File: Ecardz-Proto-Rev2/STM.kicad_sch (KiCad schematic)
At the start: 28 parts, among them J1 Conn_02x06_Odd_Even, J3 Conn_01x06, U1 STM32L071K8Ux

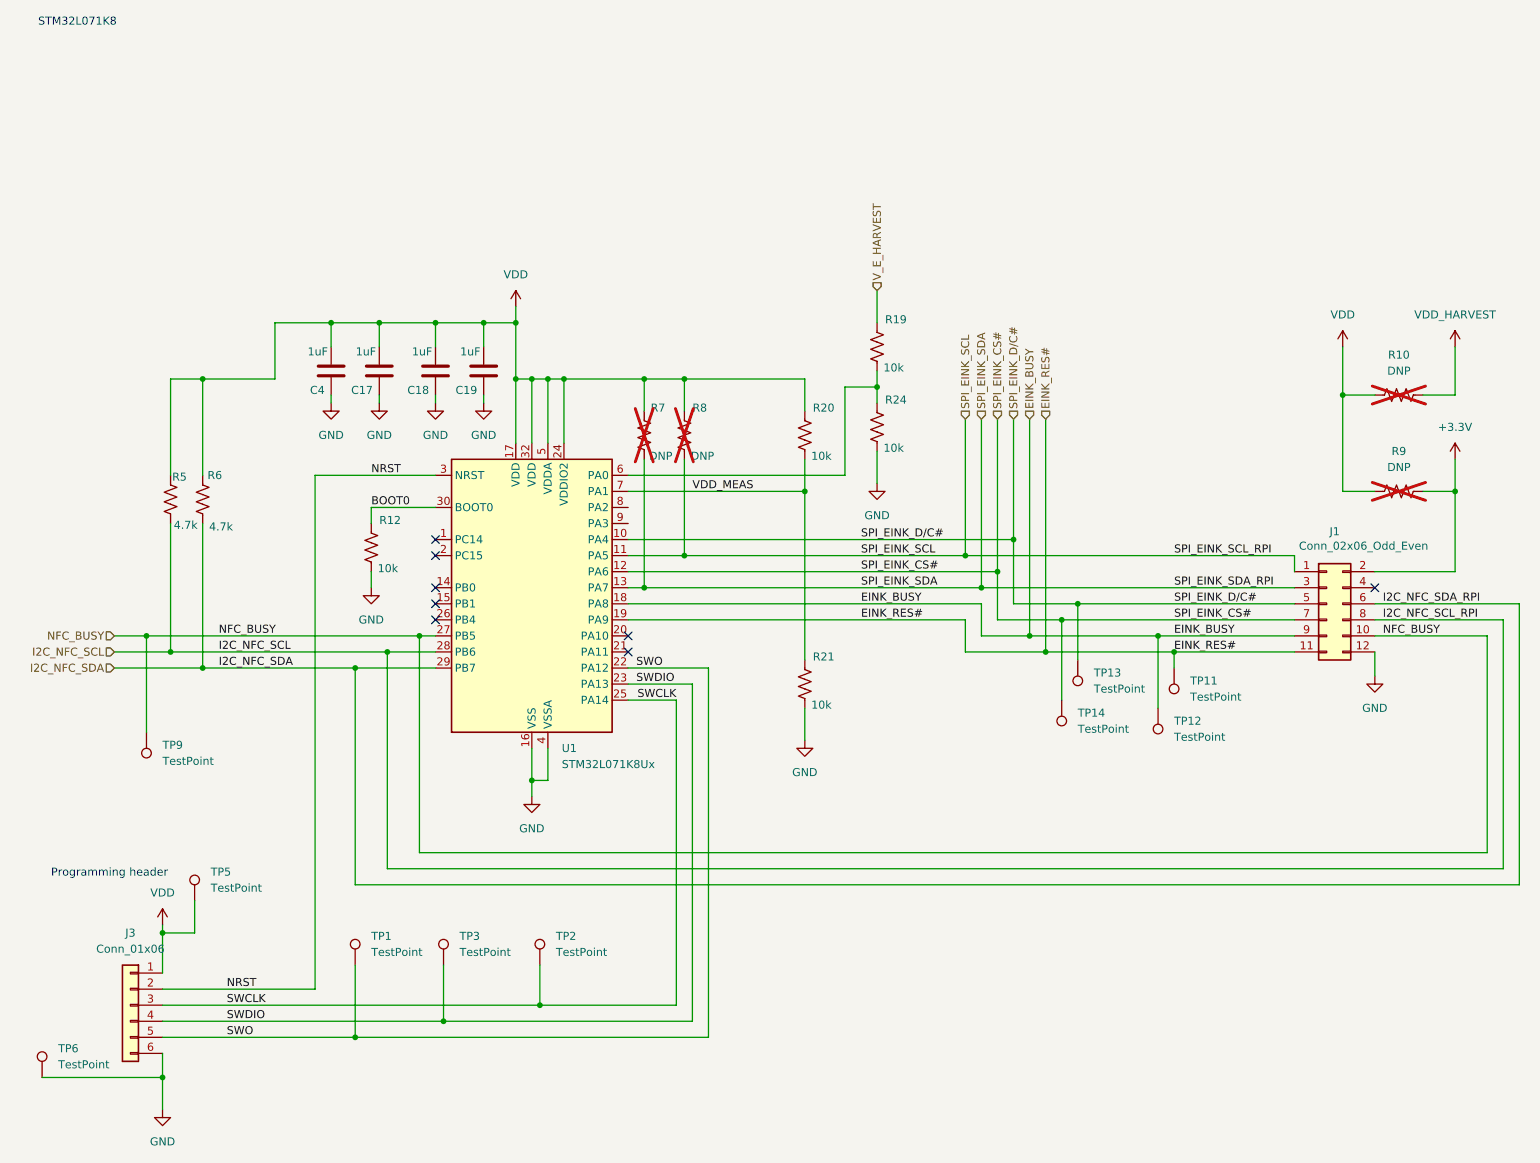
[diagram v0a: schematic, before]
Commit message: most of layout complete
switched ADC pins for ease of layout. added LEDs
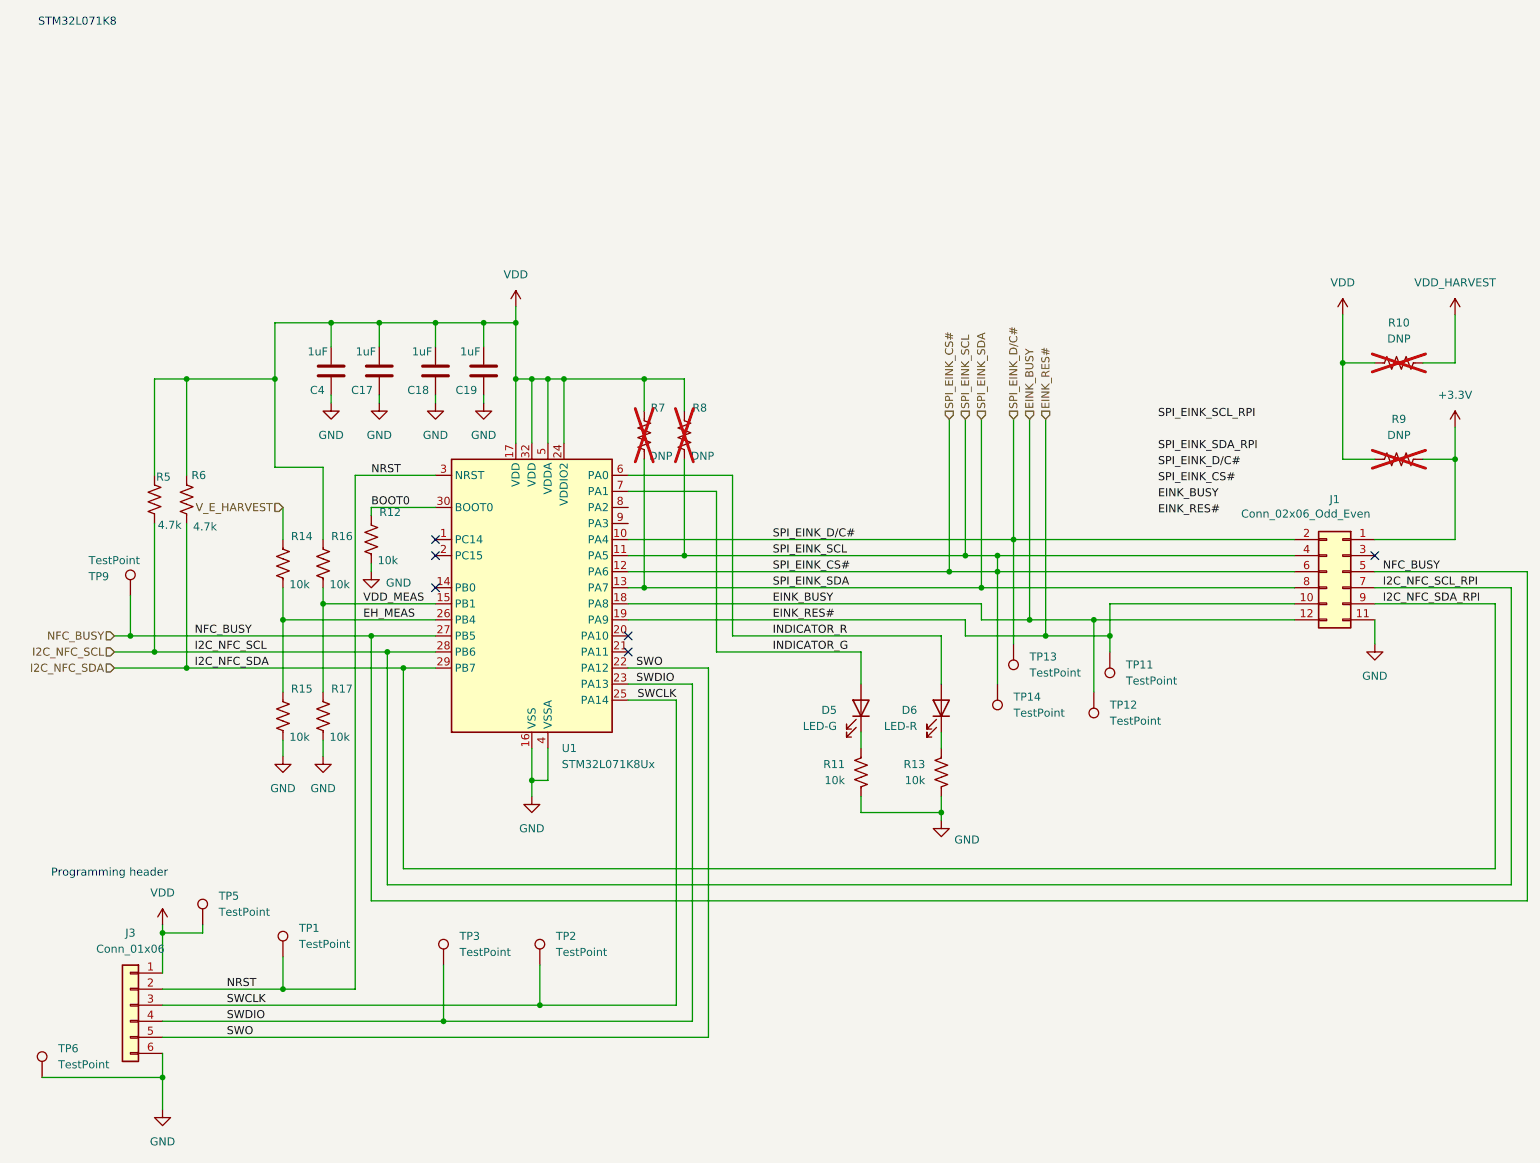
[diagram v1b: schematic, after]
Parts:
- removed R19, R20, R21, R24: 10k, Resistor_SMD:R_0603_1608Metric_Pad0.98x0.95mm_HandSolder, symbol Device:R_US
- added D5: LED-G, LED_SMD:LED_0603_1608Metric_Pad1.05x0.95mm_HandSolder, symbol Device:LED
- added D6: LED-R, LED_SMD:LED_0603_1608Metric_Pad1.05x0.95mm_HandSolder, symbol Device:LED
- added R11, R13, R14, R15, R16, R17: 10k, Resistor_SMD:R_0603_1608Metric_Pad0.98x0.95mm_HandSolder, symbol Device:R_US
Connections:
- net +3.3V: now also J1.1 (Pin_1); no longer J1.2 (Pin_2)
- net EINK_BUSY: now also J1.12 (Pin_12); no longer J1.9 (Pin_9)
- net EINK_RES#: now also J1.10 (Pin_10); no longer J1.11 (Pin_11)
- net GND: now also J1.11 (Pin_11), R11.2, R13.2, R15.2, R17.2; no longer J1.12 (Pin_12)
- net I2C_NFC_SCL: now also J1.7 (Pin_7); no longer J1.8 (Pin_8)
- net I2C_NFC_SDA: now also J1.9 (Pin_9); no longer J1.6 (Pin_6)
- net NFC_BUSY: now also J1.5 (Pin_5); no longer J1.10 (Pin_10)
- net NRST: now also TP1.1
- net SPI_EINK_CS#: now also J1.4 (Pin_4), J1.6 (Pin_6), R8.2, U1.11 (PA5); no longer J1.7 (Pin_7)
- net SPI_EINK_D/C#: now also J1.2 (Pin_2); no longer J1.5 (Pin_5)
- net SPI_EINK_SDA: now also J1.8 (Pin_8); no longer J1.3 (Pin_3)
- net SWO: no longer TP1.1
- net VDD: now also R16.1
- net VDD_MEAS: now also U1.15 (PB1), R16.2, R17.1; no longer U1.7 (PA1)
- net V_E_HARVEST: now also R14.1
- net INDICATOR_R: now reaches U1.6 (PA0)
- net INDICATOR_R: now also D6.2 (A)
- net EH_MEAS: now reaches U1.26 (PB4)
- net EH_MEAS: now also R14.2, R15.1
- removed net SPI_EINK_SCL: J1.1 (Pin_1), R8.2, U1.11 (PA5)
- new net: D6.1 (K), R13.1
- new net: D5.1 (K), R11.1
- new net INDICATOR_G: D5.2 (A), U1.7 (PA1)
- no-connect marks 8 -> 6
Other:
- moved on the sheet: R10, R12, R5, R6, R9, TP1, TP11, TP12, TP13, TP14, TP5, TP9

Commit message: removed RPI header
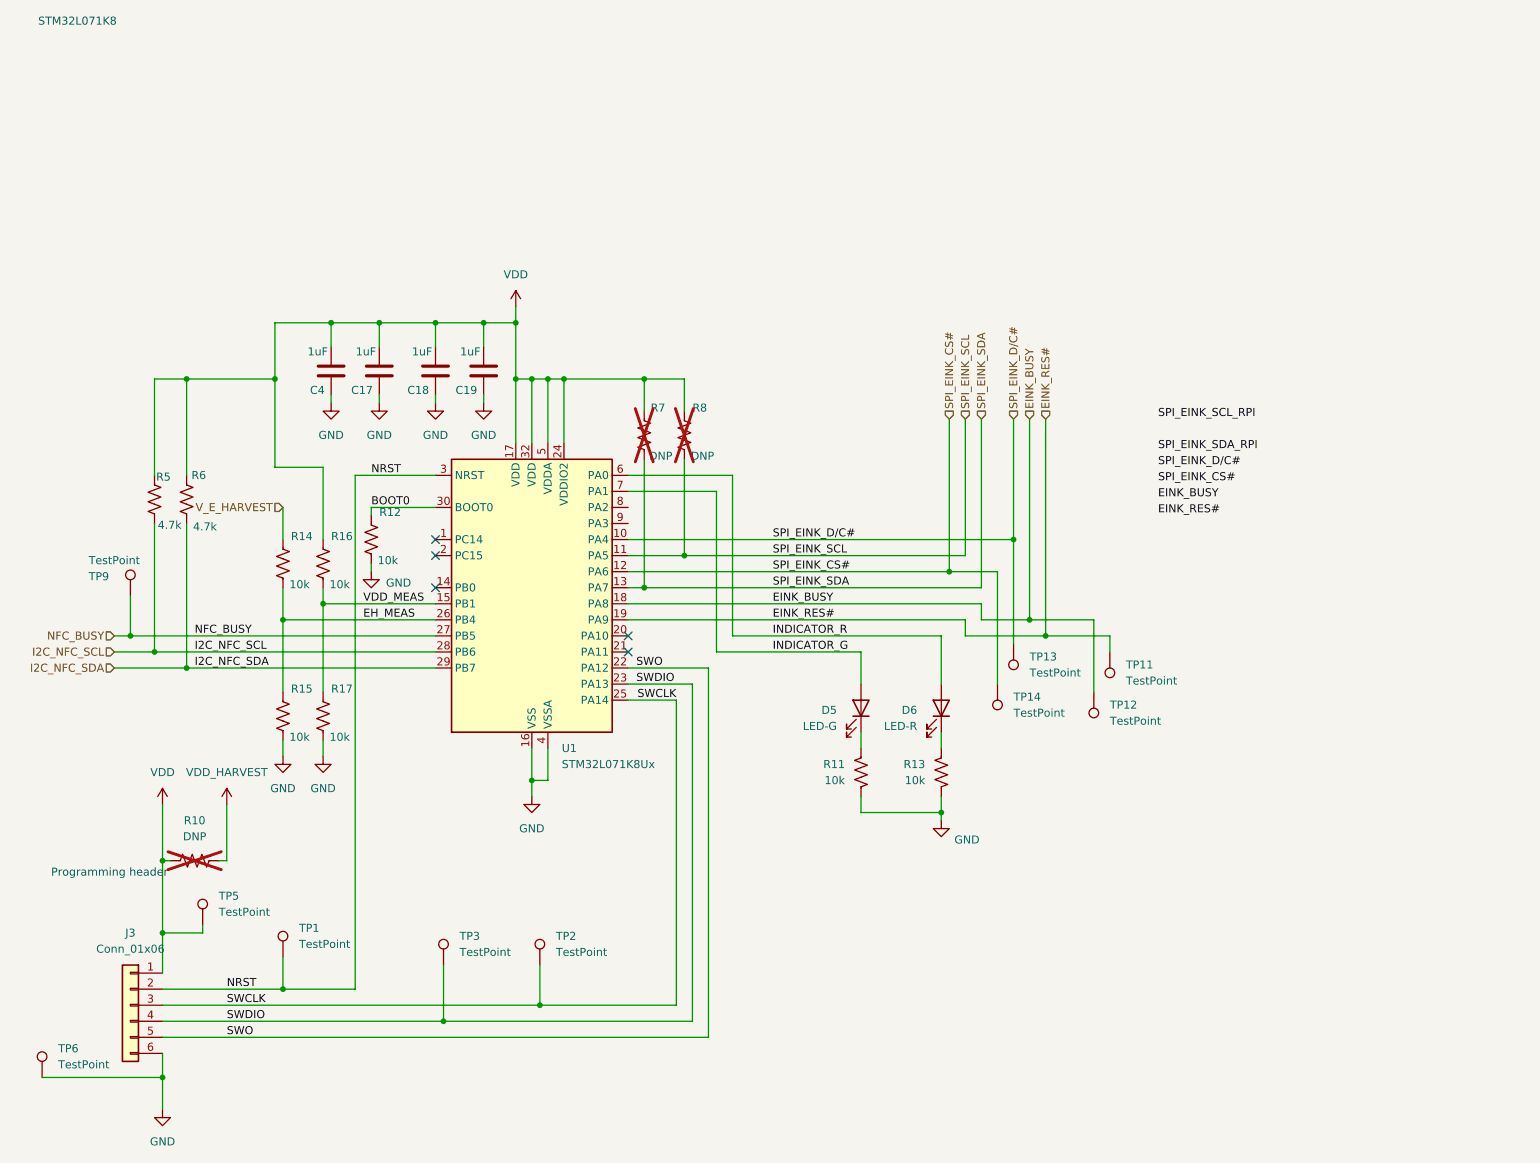
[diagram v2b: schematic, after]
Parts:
- removed J1: Conn_02x06_Odd_Even, Connector_PinHeader_2.54mm:PinHeader_2x06_P2.54mm_Vertical, symbol Connector_Generic:Conn_02x06_Odd_Even
- removed R9: DNP, Resistor_SMD:R_0603_1608Metric_Pad0.98x0.95mm_HandSolder, symbol Device:R_US
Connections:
- net SPI_EINK_CS#: no longer R8.2, U1.11 (PA5)
- new net SPI_EINK_SCL: R8.2, U1.11 (PA5)
- no-connect marks 6 -> 5
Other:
- moved on the sheet: R10

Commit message: final schematic
final schematic done and BOM generated except for pogo pins and capacitors
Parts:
- removed R5, R6: 4.7k, Resistor_SMD:R_0603_1608Metric_Pad0.98x0.95mm_HandSolder, symbol Device:R_US
- added J1, J4: Conn_01x02, symbol Connector_Generic:Conn_01x02
- D5: MANUFACTURER PART NUMBER (none) -> 150060GS75000; Part Number 150060GS75000 -> (none)
- D6: MANUFACTURER PART NUMBER (none) -> 150060RS75000; Part Number 150060RS75000 -> (none)
- J3: now not fitted
- R10: now fitted
- R11, R13: MANUFACTURER PART NUMBER (none) -> RC0603FR-0710KL
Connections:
- net GND: now also J1.1 (Pin_1)
- net VDD: now also J1.2 (Pin_2), J4.2 (Pin_2)
- net VDD_HARVEST: now also J4.1 (Pin_1)
- net NFC_POWER: now reaches U1.14 (PB0)
- net EINK_POWER_CTRL_N: now reaches U1.9 (PA3)
- no-connect marks 5 -> 4
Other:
- moved on the sheet: R12, R14, R16, TP9

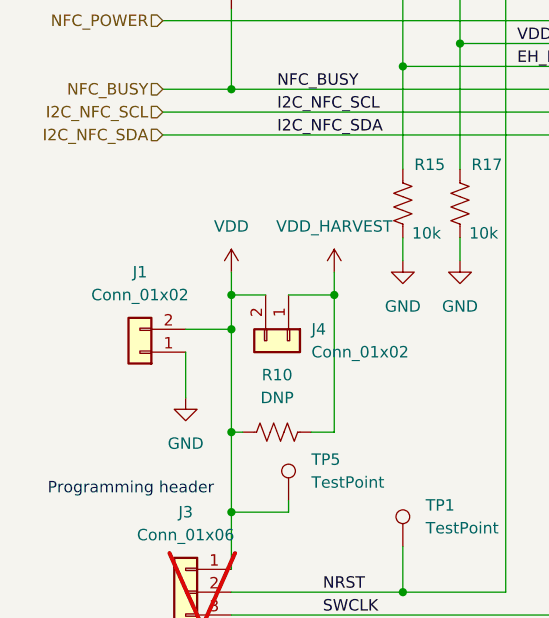
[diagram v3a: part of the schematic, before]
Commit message: initial fit check for mech
final footprints defined and placement is mostly complete
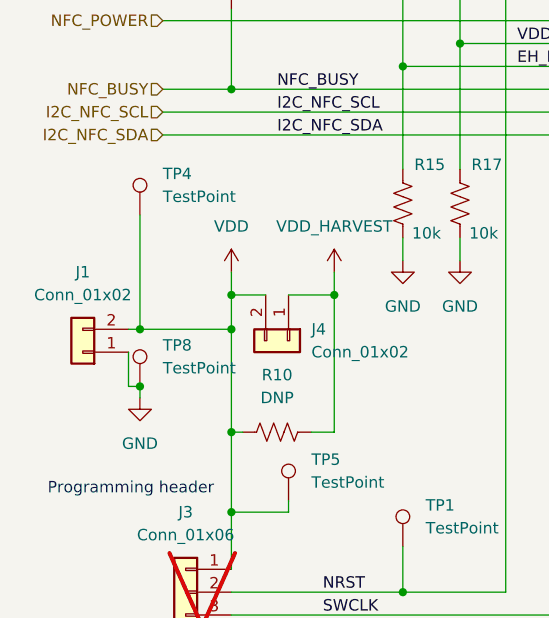
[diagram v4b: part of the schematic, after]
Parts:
- added TP4, TP8: TestPoint, TestPoint:TestPoint_Pad_D1.5mm, symbol Connector:TestPoint
- J1, J4: footprint (none) -> Connector_PinHeader_2.54mm:PinHeader_1x02_P2.54mm_Vertical
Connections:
- net GND: now also TP8.1
- net VDD: now also TP4.1
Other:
- moved on the sheet: J1
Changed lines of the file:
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@@
 	)
 	(junction
+		(at 24.13 147.32)
+		(diameter 0)
+		(color 0 0 0 0)
+	)
+	(junction
 		(at 110.49 73.66)
 		(diameter 0)
@@
 	)
 	(junction
+		(at 24.13 140.97)
+		(diameter 0)
+		(color 0 0 0 0)
+	)
+	(junction
 		(at 90.17 64.77)
 		(diameter 0)
@@
 	(wire
 		(pts
+			(xy 22.86 147.32) (xy 22.86 143.51)
+		)
+		(stroke
+			(width 0)
+			(type default)
+		)
+	)
+	(wire
+		(pts
 			(xy 144.78 116.84) (xy 121.92 116.84)
 		)
@@
 	(wire
 		(pts
+			(xy 24.13 128.27) (xy 24.13 140.97)
+		)
+		(stroke
+			(width 0)
+			(type default)
+		)
+	)
+	(wire
+		(pts
 			(xy 161.29 111.76) (xy 161.29 114.3)
 		)
@@
 	(wire
 		(pts
+			(xy 24.13 140.97) (xy 34.29 140.97)
+		)
+		(stroke
+			(width 0)
+			(type default)
+		)
+	)
+	(wire
+		(pts
 			(xy 34.29 137.16) (xy 34.29 140.97)
 		)
@@
 	(wire
 		(pts
-			(xy 29.21 148.59) (xy 29.21 143.51)
+			(xy 24.13 148.59) (xy 24.13 147.32)
 		)
 		(stroke
@@
 	(wire
 		(pts
-			(xy 29.21 140.97) (xy 34.29 140.97)
+			(xy 22.86 140.97) (xy 24.13 140.97)
 		)
 		(stroke
@@
 	(wire
 		(pts
+			(xy 24.13 147.32) (xy 22.86 147.32)
+		)
+		(stroke
+			(width 0)
+			(type default)
+		)
+	)
+	(wire
+		(pts
 			(xy 93.98 166.37) (xy 93.98 172.72)
 		)
@@
 	)
 	(symbol
+		(lib_id "Connector:TestPoint")
+		(at 24.13 147.32 0)
+		(unit 1)
+		(exclude_from_sim no)
+		(in_bom yes)
+		(on_board yes)
+		(dnp no)
+		(fields_autoplaced yes)
+		(property "Reference" "TP8"
+			(at 26.67 142.7479 0)
+			(effects
+				(font
+					(size 1.27 1.27)
+				)
+				(justify left)
+			)
+		)
+		(property "Value" "TestPoint"
+			(at 26.67 145.2879 0)
+			(effects
+				(font
+					(size 1.27 1.27)
+				)
+				(justify left)
+			)
+		)
+		(property "Footprint" "TestPoint:TestPoint_Pad_D1.5mm"
+			(at 29.21 147.32 0)
+			(effects
+				(font
+					(size 1.27 1.27)
+				)
+				(hide yes)
+			)
+		)
+		(property "Datasheet" "~"
+			(at 29.21 147.32 0)
+			(effects
+				(font
+					(size 1.27 1.27)
+				)
+				(hide yes)
+			)
+		)
+		(property "Description" "test point"
+			(at 24.13 147.32 0)
+			(effects
+				(font
+					(size 1.27 1.27)
+				)
+				(hide yes)
+			)
+		)
+		(property "Digikey Part Number" ""
+			(at 24.13 147.32 0)
+			(effects
+				(font
+					(size 1.27 1.27)
+				)
+				(hide yes)
+			)
+		)
+		(pin "1"
+		)
+		(instances
+			(project "Ecardz-Proto"
+				(path "/2adbba85-9270-4efb-857d-656bb51406ca/fb28d19f-d7f8-44fd-bba1-2dc19a83839b"
+					(reference "TP8")
+					(unit 1)
+				)
+			)
+		)
+	)
+	(symbol
 		(lib_id "power:GND")
 		(at 59.69 133.35 0)
@@
 	(symbol
 		(lib_id "Connector_Generic:Conn_01x02")
-		(at 24.13 143.51 180)
+		(at 17.78 143.51 180)
 		(unit 1)
 		(exclude_from_sim no)
@@
 		(fields_autoplaced yes)
 		(property "Reference" "J1"
-			(at 24.13 134.62 0)
+			(at 17.78 134.62 0)
 			(effects
 				(font
@@
 		)
 		(property "Value" "Conn_01x02"
-			(at 24.13 137.16 0)
+			(at 17.78 137.16 0)
 			(effects
 				(font
@@
 			)
 		)
-		(property "Footprint" ""
-			(at 24.13 143.51 0)
+		(property "Footprint" "Connector_PinHeader_2.54mm:PinHeader_1x02_P2.54mm_Vertical "
+			(at 17.78 143.51 0)
 			(effects
 				(font
@@
 		)
 		(property "Datasheet" "~"
-			(at 24.13 143.51 0)
+			(at 17.78 143.51 0)
 			(effects
 				(font
@@
 		)
 		(property "Description" "Generic connector, single row, 01x02, script generated (kicad-library-utils/schlib/autogen/connector/)"
-			(at 24.13 143.51 0)
+			(at 17.78 143.51 0)
 			(effects
 				(font
@@
 	(symbol
 		(lib_id "power:GND")
-		(at 29.21 148.59 0)
+		(at 24.13 148.59 0)
 		(unit 1)
 		(exclude_from_sim no)
@@
 		(fields_autoplaced yes)
 		(property "Reference" "#PWR09"
-			(at 29.21 154.94 0)
+			(at 24.13 154.94 0)
 			(effects
 				(font
@@
 		)
 		(property "Value" "GND"
-			(at 29.21 153.67 0)
+			(at 24.13 153.67 0)
 			(effects
 				(font
@@
 		)
 		(property "Footprint" ""
-			(at 29.21 148.59 0)
+			(at 24.13 148.59 0)
 			(effects
 				(font
@@
 		)
 		(property "Datasheet" ""
-			(at 29.21 148.59 0)
+			(at 24.13 148.59 0)
 			(effects
 				(font
@@
 		)
 		(property "Description" "Power symbol creates a global label with name \"GND\" , ground"
-			(at 29.21 148.59 0)
+			(at 24.13 148.59 0)
 			(effects
 				(font
@@
 			)
 		)
-		(property "Footprint" ""
+		(property "Footprint" "Connector_PinHeader_2.54mm:PinHeader_1x02_P2.54mm_Vertical"
 			(at 40.64 142.24 0)
 			(effects
@@
 					(unit 1)
 				)
+			)
+		)
+	)
+	(symbol
+		(lib_id "Connector:TestPoint")
+		(at 24.13 128.27 0)
+		(unit 1)
+		(exclude_from_sim no)
+		(in_bom yes)
+		(on_board yes)
+		(dnp no)
+		(fields_autoplaced yes)
+		(property "Reference" "TP4"
+			(at 26.67 123.6979 0)
+			(effects
+				(font
+					(size 1.27 1.27)
+				)
+				(justify left)
+			)
+		)
+		(property "Value" "TestPoint"
+			(at 26.67 126.2379 0)
+			(effects
+				(font
+					(size 1.27 1.27)
+				)
+				(justify left)
+			)
+		)
+		(property "Footprint" "TestPoint:TestPoint_Pad_D1.5mm"
+			(at 29.21 128.27 0)
+			(effects
+				(font
+					(size 1.27 1.27)
+				)
+				(hide yes)
+			)
+		)
+		(property "Datasheet" "~"
+			(at 29.21 128.27 0)
+			(effects
+				(font
+					(size 1.27 1.27)
+				)
+				(hide yes)
+			)
+		)
+		(property "Description" "test point"
+			(at 24.13 128.27 0)
+			(effects
+				(font
+					(size 1.27 1.27)
+				)
+				(hide yes)
+			)
+		)
+		(property "Digikey Part Number" ""
+			(at 24.13 128.27 0)
+			(effects
+				(font
+					(size 1.27 1.27)
+				)
+				(hide yes)
+			)
+		)
+		(pin "1"
+		)
+		(instances
+			(project "Ecardz-Proto"
+				(path "/2adbba85-9270-4efb-857d-656bb51406ca/fb28d19f-d7f8-44fd-bba1-2dc19a83839b"
+					(reference "TP4")
+					(unit 1)
+				)

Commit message: second mech spin
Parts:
- J1: footprint Connector_PinHeader_2.54mm:PinHeader_1x02_P2.54mm_Vertical -> Connector_PinHeader_2.54mm:PinHeader_1x02_P2.54mm_Vertical; now not fitted
- J4: now not fitted
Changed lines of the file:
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@@
 		(in_bom yes)
 		(on_board yes)
-		(dnp no)
+		(dnp yes)
 		(fields_autoplaced yes)
 		(property "Reference" "J1"
@@
 			)
 		)
-		(property "Footprint" "Connector_PinHeader_2.54mm:PinHeader_1x02_P2.54mm_Vertical "
+		(property "Footprint" "Connector_PinHeader_2.54mm:PinHeader_1x02_P2.54mm_Vertical"
 			(at 17.78 143.51 0)
 			(effects
@@
 		(in_bom yes)
 		(on_board yes)
-		(dnp no)
+		(dnp yes)
 		(fields_autoplaced yes)
 		(property "Reference" "J4"
